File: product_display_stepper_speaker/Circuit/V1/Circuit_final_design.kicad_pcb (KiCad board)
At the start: 2 copper layers, 90.9 x 52.4 mm, 21 parts, among them J1 Barrel_Jack_MountingPin, U1 L7805, U2 LD33v, U3 ESP-12E

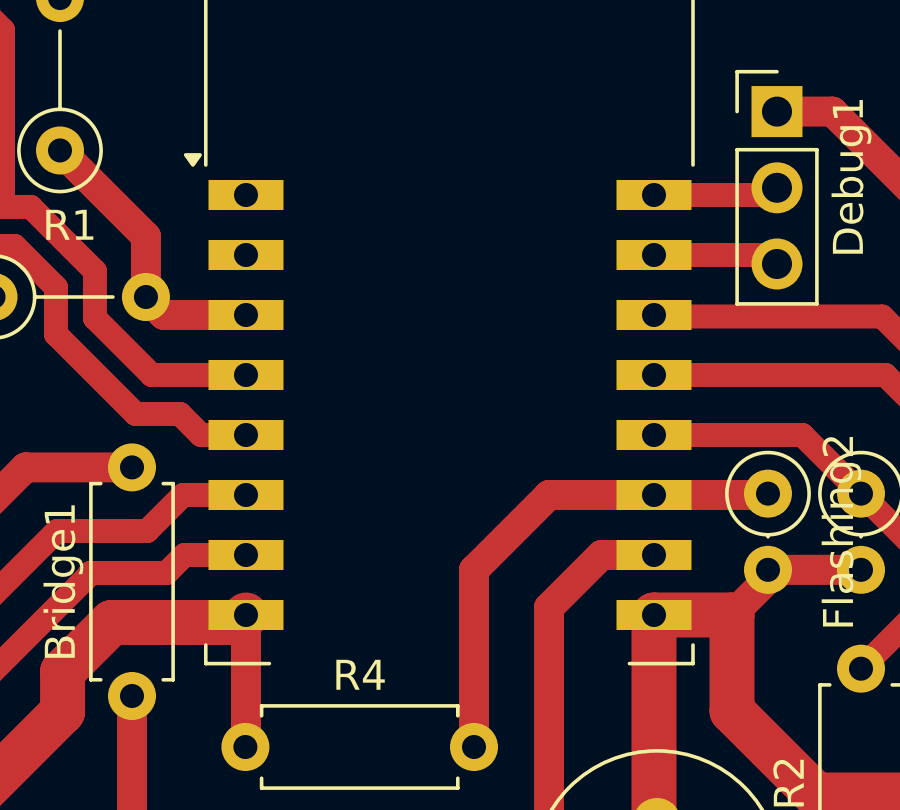
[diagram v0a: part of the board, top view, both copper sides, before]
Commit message: started V2 of this project, gonna use Pico w instead of esp-12e
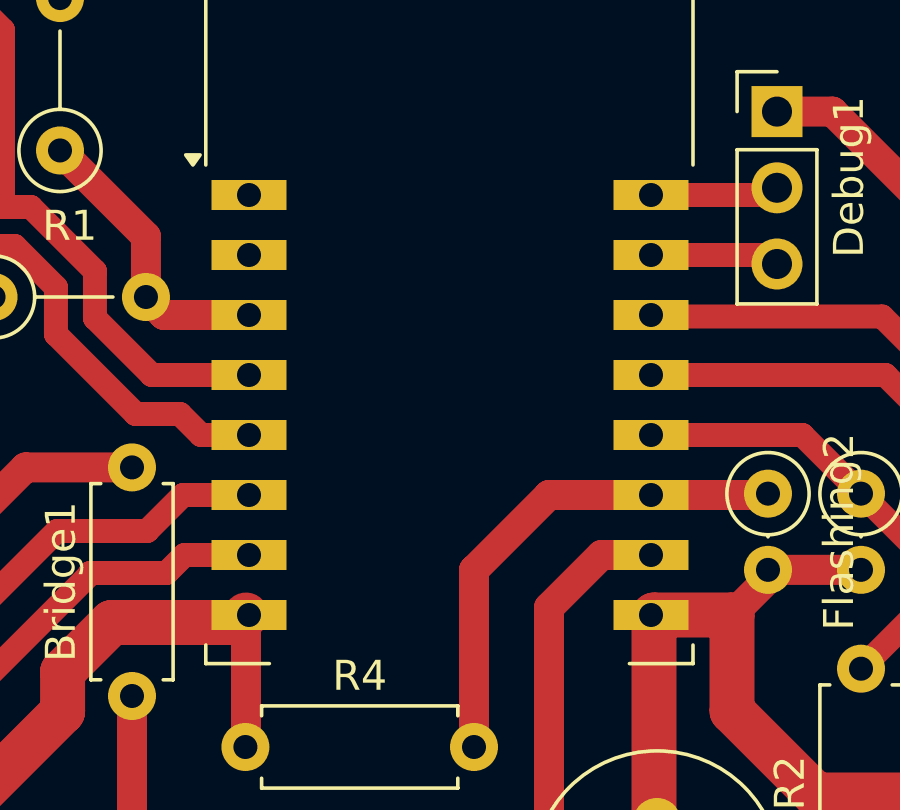
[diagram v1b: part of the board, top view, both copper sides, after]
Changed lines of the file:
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@@
 		)
 		(pad "1" thru_hole rect
-			(at -6.8 -4.2)
+			(at -6.7 -4.2)
 			(size 2.5 1)
 			(drill 0.8)
@@
 		)
 		(pad "2" thru_hole rect
-			(at -6.8 -2.2)
+			(at -6.7 -2.2)
 			(size 2.5 1)
 			(drill 0.8)
@@
 		)
 		(pad "3" thru_hole rect
-			(at -6.8 -0.2)
+			(at -6.7 -0.2)
 			(size 2.5 1)
 			(drill 0.8)
@@
 		)
 		(pad "4" thru_hole rect
-			(at -6.8 1.8)
+			(at -6.7 1.8)
 			(size 2.5 1)
 			(drill 0.8)
@@
 		)
 		(pad "5" thru_hole rect
-			(at -6.8 3.8)
+			(at -6.7 3.8)
 			(size 2.5 1)
 			(drill 0.8)
@@
 		)
 		(pad "6" thru_hole rect
-			(at -6.8 5.8)
+			(at -6.7 5.8)
 			(size 2.5 1)
 			(drill 0.8)
@@
 		)
 		(pad "7" thru_hole rect
-			(at -6.8 7.8)
+			(at -6.7 7.8)
 			(size 2.5 1)
 			(drill 0.8)
@@
 		)
 		(pad "8" thru_hole rect
-			(at -6.8 9.8)
+			(at -6.7 9.8)
 			(size 2.5 1)
 			(drill 0.8)
@@
 		)
 		(pad "15" thru_hole rect
-			(at 6.8 9.8)
+			(at 6.7 9.8)
 			(size 2.5 1)
 			(drill 0.8)
@@
 		)
 		(pad "16" thru_hole rect
-			(at 6.8 7.8)
+			(at 6.7 7.8)
 			(size 2.5 1)
 			(drill 0.8)
@@
 		)
 		(pad "17" thru_hole rect
-			(at 6.8 5.8)
+			(at 6.7 5.8)
 			(size 2.5 1)
 			(drill 0.8)
@@
 		)
 		(pad "18" thru_hole rect
-			(at 6.8 3.8)
+			(at 6.7 3.8)
 			(size 2.5 1)
 			(drill 0.8)
@@
 		)
 		(pad "19" thru_hole rect
-			(at 6.8 1.8)
+			(at 6.7 1.8)
 			(size 2.5 1)
 			(drill 0.8)
@@
 		)
 		(pad "20" thru_hole rect
-			(at 6.8 -0.2)
+			(at 6.7 -0.2)
 			(size 2.5 1)
 			(drill 0.8)
@@
 		)
 		(pad "21" thru_hole rect
-			(at 6.8 -2.2)
+			(at 6.7 -2.2)
 			(size 2.5 1)
 			(drill 0.8)
@@
 		)
 		(pad "22" thru_hole rect
-			(at 6.8 -4.2)
+			(at 6.7 -4.2)
 			(size 2.5 1)
 			(drill 0.8)
